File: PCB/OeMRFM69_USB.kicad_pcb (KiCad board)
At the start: 2 copper layers, 42 x 28 mm, 24 parts, among them J1 AERIAL, J2 TYPE-C-31-M-12, U1 ATtiny1624-SS, U2 RFM69CW, U4 XC6206-3.3V, U5 CH340C

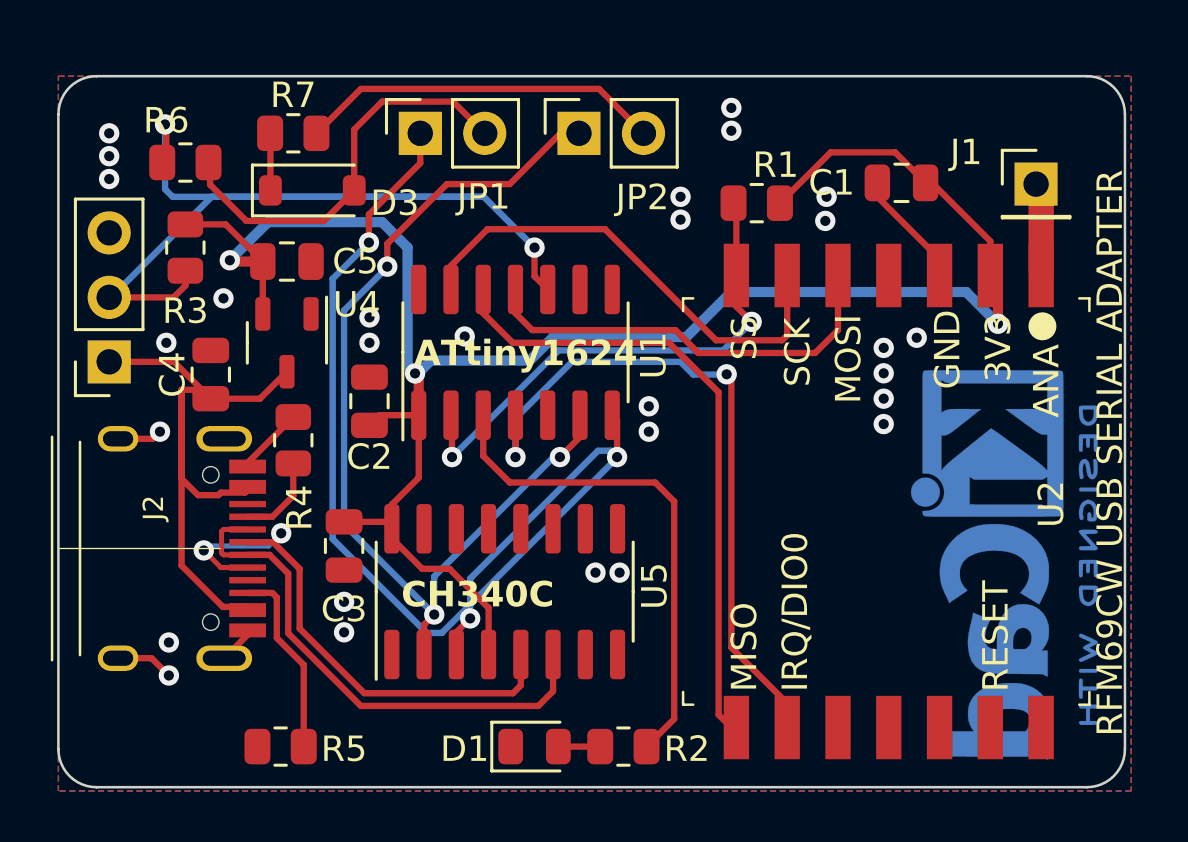
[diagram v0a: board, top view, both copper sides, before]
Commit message: Add hash silkscreen stamp
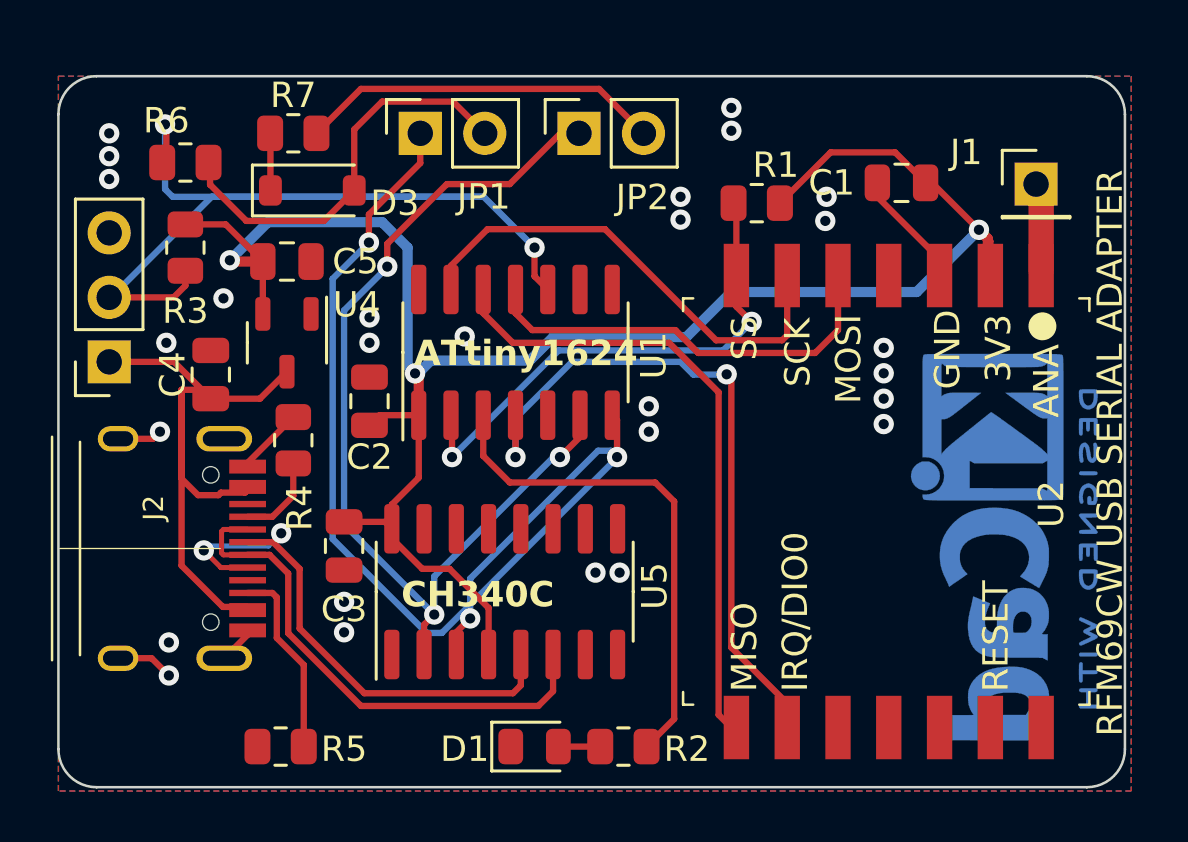
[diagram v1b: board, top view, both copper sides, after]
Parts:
- moved REF** 0.64 mm to (147.1, 96.1)
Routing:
- net +3V3: track 76.5 -> 76.0 mm
- net GND: vias 28 -> 27
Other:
- board text added: "<<date>>"
- board text added: "<<hash>>"

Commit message: Updated BOM
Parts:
- JP1, JP2: footprint Connector_PinSocket_2.54mm:PinSocket_1x02_P2.54mm_Vertical -> Connector_PinHeader_2.54mm:PinHeader_1x02_P2.54mm_Vertical

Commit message: RFM69 footprint changes
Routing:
- net Net-(U1-PA3): track 19.0 -> 20.7 mm
- net /UPDI: track 41.3 -> 42.3 mm
- net +3V3: track 76.0 -> 77.0 mm
- net Net-(U1-PA4): track 20.4 -> 19.4 mm
- net Net-(J1-Pin_1): track 3.48 -> 4.24 mm
- net GND: track 12.4 -> 13.1 mm
- net /INT: track 27.0 -> 26.5 mm
